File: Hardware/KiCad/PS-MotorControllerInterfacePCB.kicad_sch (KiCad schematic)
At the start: 52 parts, among them J5 53307-2471

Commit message: finished LCSC
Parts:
- added GND1: TP_GND, Connector_PinHeader_2.54mm:PinHeader_1x01_P2.54mm_Vertical, symbol Connector:TestPoint
- 12VSNS1, 24V1, 3V3, BUCK_OUT1, CAN(board->moco,mppts)1, CAN(moco,mppts->board)1, CANDAPTER1, CAN_IN1, CAN_OUT1, FAULT1, HSS_EN1, I_MOTOR1, PP_OUT1, PWR_12V1, PWR_BOARD1, STATUS1, SW_OC1, TP_1, TP_2: now left out of the parts list
- F_10A: renamed from F1; LCSC (none) -> C5249699
- GND2: renamed from TP1; now left out of the parts list
- LED1, LED11, LED2, LED3, LED4, LED5, LED6, LED7, LED8, LED9, LVPWR1: LCSC (none) -> C7371904
- R1, R2, R3, R32, R5, R6, R7, R8: LCSC C2907165 -> C21190
- R25, R30, R34: LCSC (none) -> C21189
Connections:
- net GND: now also GND1.1

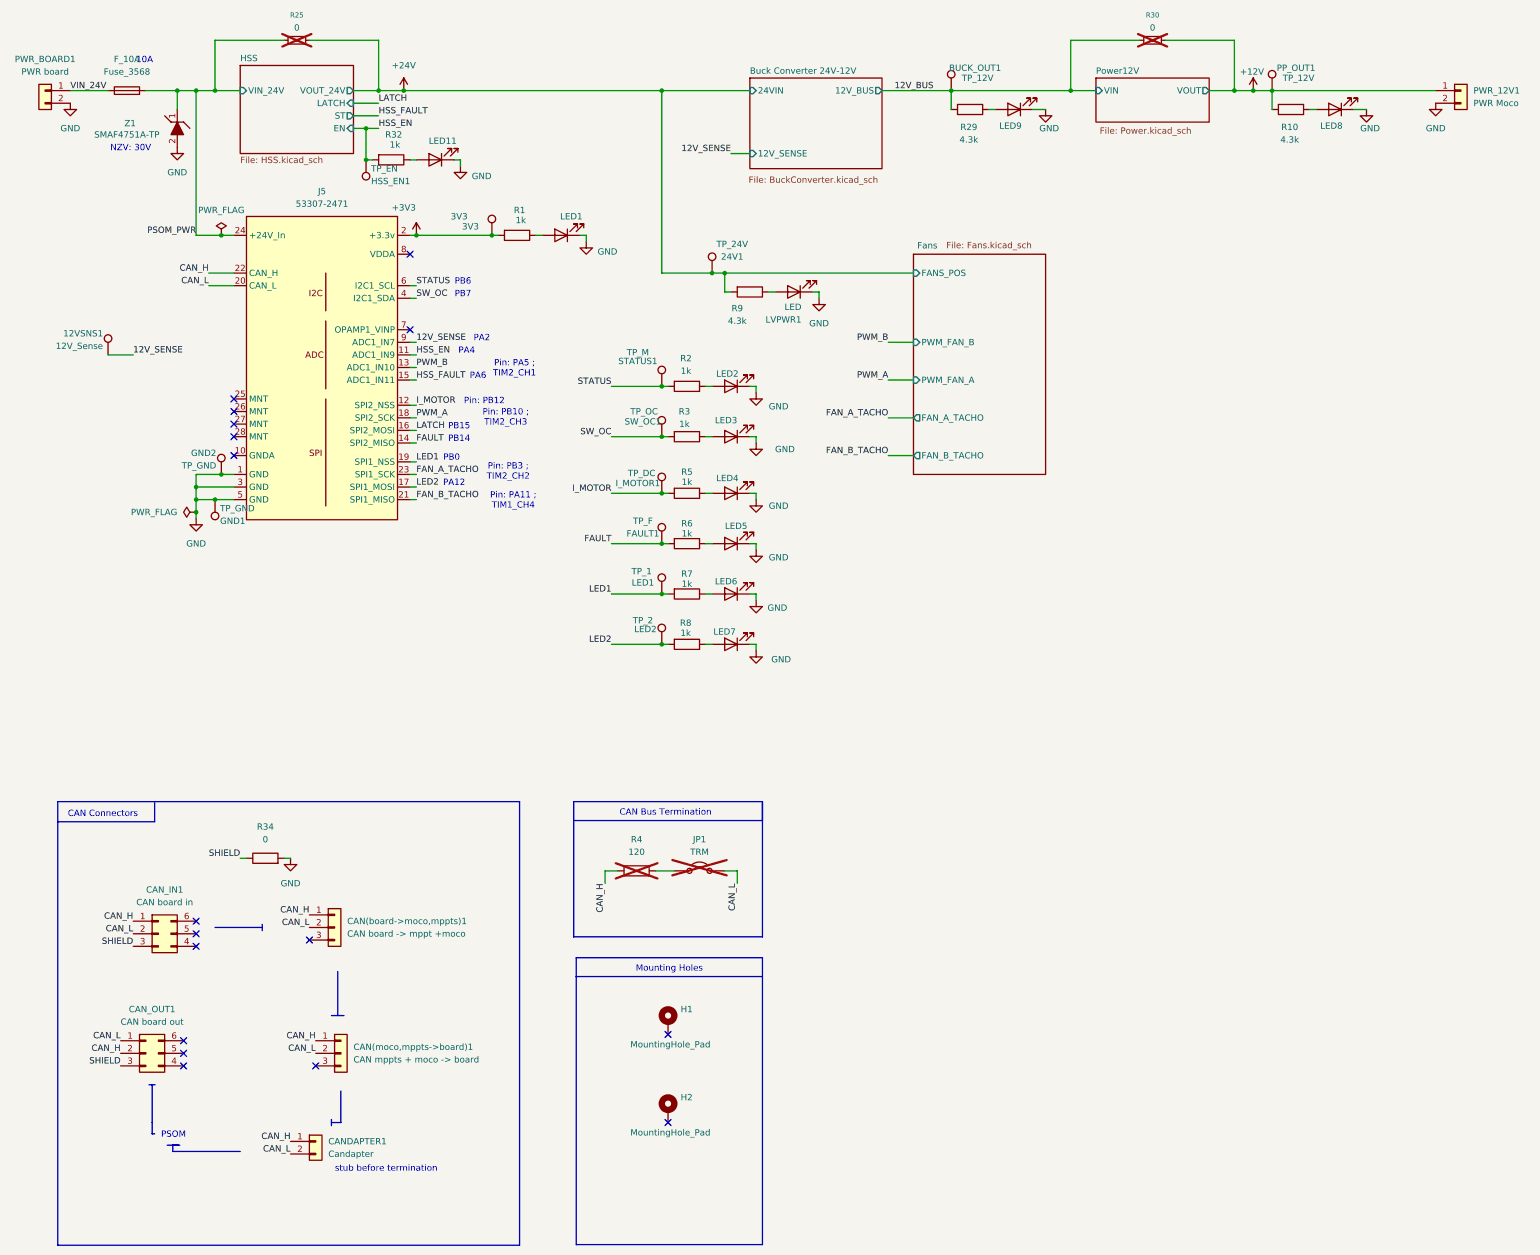
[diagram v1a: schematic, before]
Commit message: fixed references and changed the labels
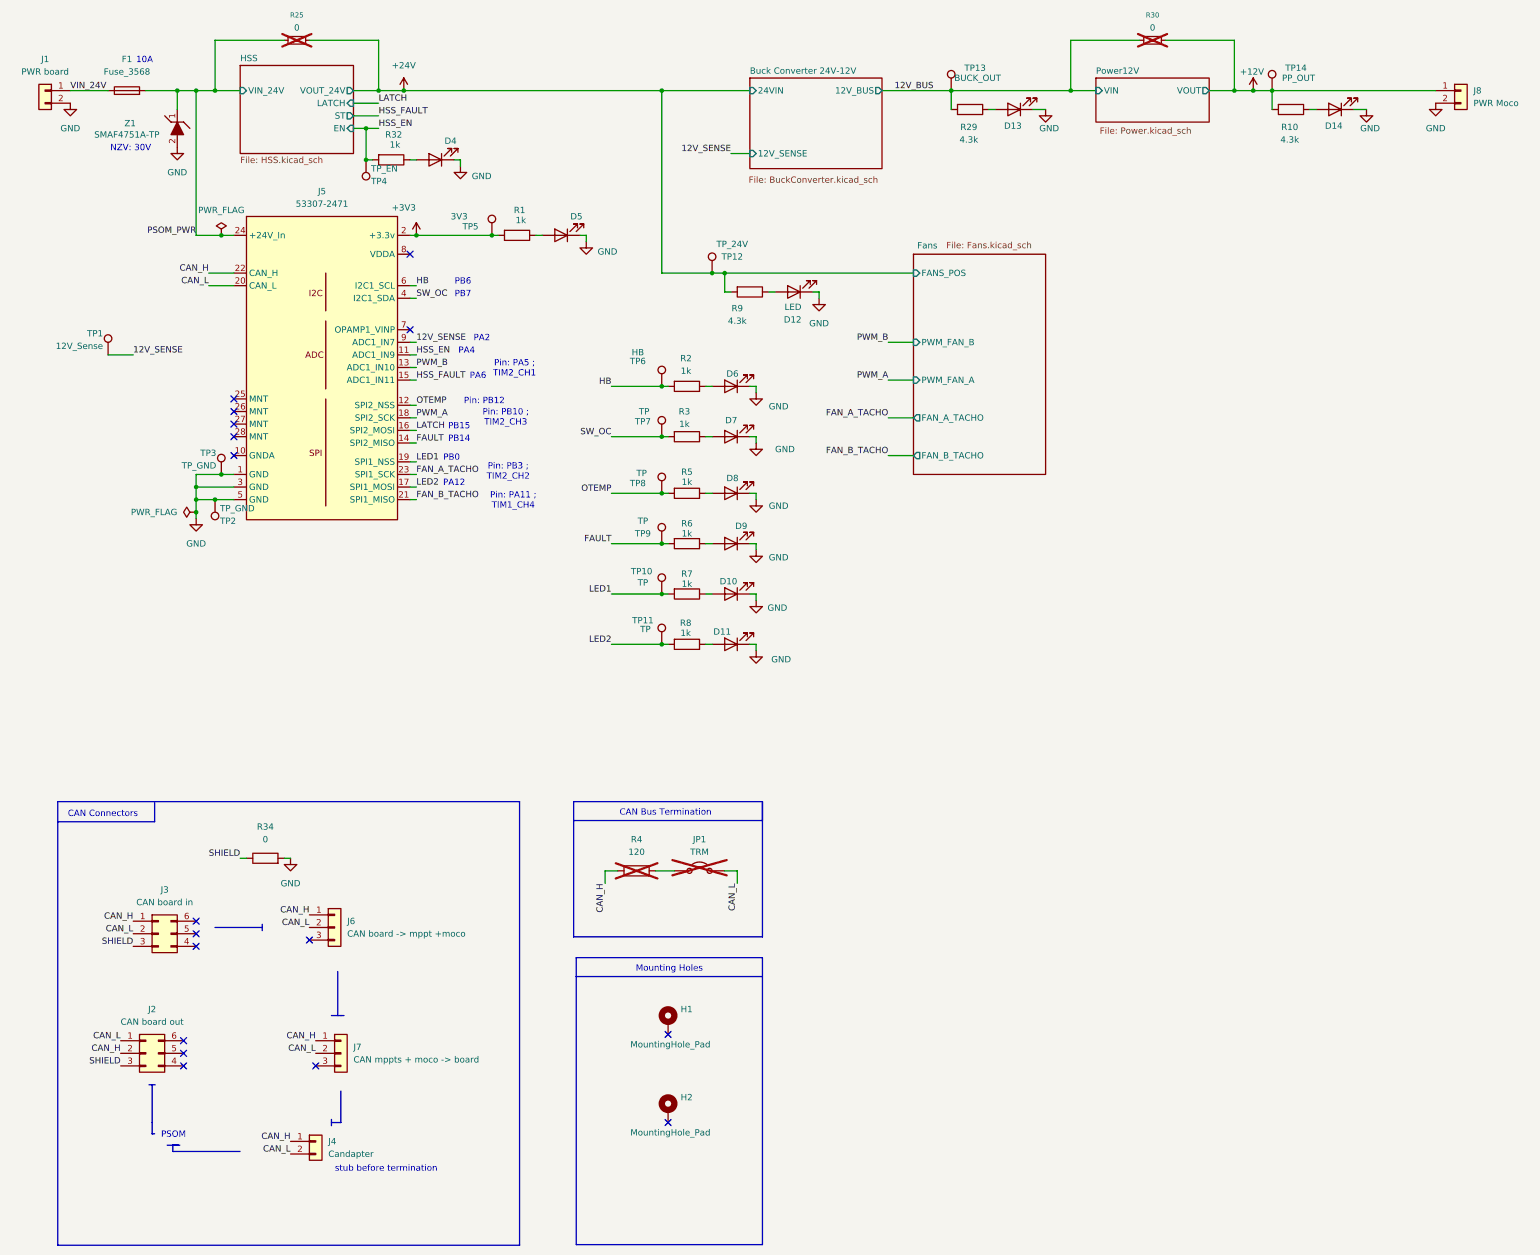
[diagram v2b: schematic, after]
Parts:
- TP10: renamed from TP_1; value LED1 -> TP
- TP11: renamed from TP_2; value LED2 -> TP
- TP13: renamed from BUCK_OUT1; value TP_12V -> BUCK_OUT
- TP14: renamed from PP_OUT1; value TP_12V -> PP_OUT
- TP6: renamed from STATUS1; value TP_M -> HB
- TP7: renamed from SW_OC1; value TP_OC -> TP
- TP8: renamed from I_MOTOR1; value TP_DC -> TP
- TP9: renamed from FAULT1; value TP_F -> TP
- renumbered LED6 to D10, LED7 to D11, LVPWR1 to D12, LED9 to D13, LED8 to D14, LED11 to D4, LED1 to D5, LED2 to D6, LED3 to D7, LED4 to D8, LED5 to D9, F_10A to F1, PWR_BOARD1 to J1, CAN_OUT1 to J2, CAN_IN1 to J3, CANDAPTER1 to J4, CAN(board->moco,mppts)1 to J6, CAN(moco,mppts->board)1 to J7, PWR_12V1 to J8, 12VSNS1 to TP1, 24V1 to TP12, GND1 to TP2, GND2 to TP3, HSS_EN1 to TP4, 3V3 to TP5
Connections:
- net I_MOTOR renamed OTEMP
- net STATUS renamed HB

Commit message: standardized some lcsc
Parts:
- D10, D11, D12, D13, D14, D4, D5, D6, D7, D8, D9: LCSC C7371904 -> C84263
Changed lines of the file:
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@@
 			)
 		)
-		(property "LCSC" "C7371904"
+		(property "LCSC" "C84263"
 			(at 180.34 134.62 90)
 			(effects
@@
 			)
 		)
-		(property "LCSC" "C7371904"
+		(property "LCSC" "C84263"
 			(at 180.34 92.71 90)
 			(effects
@@
 			)
 		)
-		(property "LCSC" "C7371904"
+		(property "LCSC" "C84263"
 			(at 302.26 36.83 90)
 			(effects
@@
 			)
 		)
-		(property "LCSC" "C7371904"
+		(property "LCSC" "C84263"
 			(at 146.05 62.23 90)
 			(effects
@@
 			)
 		)
-		(property "LCSC" "C7371904"
+		(property "LCSC" "C84263"
 			(at 237.49 36.83 90)
 			(effects
@@
 			)
 		)
-		(property "LCSC" "C7371904"
+		(property "LCSC" "C84263"
 			(at 180.34 114.3 90)
 			(effects
@@
 			)
 		)
-		(property "LCSC" "C7371904"
+		(property "LCSC" "C84263"
 			(at 120.65 46.99 90)
 			(effects
@@
 			)
 		)
-		(property "LCSC" "C7371904"
+		(property "LCSC" "C84263"
 			(at 180.34 124.46 90)
 			(effects
@@
 			)
 		)
-		(property "LCSC" "C7371904"
+		(property "LCSC" "C84263"
 			(at 180.34 144.78 90)
 			(effects
@@
 			)
 		)
-		(property "LCSC" "C7371904"
+		(property "LCSC" "C84263"
 			(at 180.34 102.87 90)
 			(effects
@@
 			)
 		)
-		(property "LCSC" "C7371904"
+		(property "LCSC" "C84263"
 			(at 193.04 73.66 90)
 			(effects
